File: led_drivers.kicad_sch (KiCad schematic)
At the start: 7 parts, among them Q1 MMBT3904

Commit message: routing done
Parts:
- renumbered Q1 to Q6, R4 to R43, R5 to R44, R6 to R45, R7 to R46, R8 to R47, R18 to R48
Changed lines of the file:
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@@
   (symbol (lib_id "Device:R") (at 109.22 59.055 0) (unit 1)
     (in_bom yes) (on_board yes) (fields_autoplaced)
-    (property "Reference" "R18" (id 0) (at 110.998 58.2203 0)
+    (property "Reference" "R48" (id 0) (at 110.998 58.2203 0)
       (effects (font (size 1.27 1.27)) (justify left))
     )
@@
   (symbol (lib_id "Device:R") (at 71.12 59.055 0) (unit 1)
     (in_bom yes) (on_board yes) (fields_autoplaced)
-    (property "Reference" "R5" (id 0) (at 72.898 58.2203 0)
+    (property "Reference" "R44" (id 0) (at 72.898 58.2203 0)
       (effects (font (size 1.27 1.27)) (justify left))
     )
@@
   (symbol (lib_id "Device:R") (at 59.69 67.945 90) (unit 1)
     (in_bom yes) (on_board yes) (fields_autoplaced)
-    (property "Reference" "R4" (id 0) (at 59.69 70.9914 90))
+    (property "Reference" "R43" (id 0) (at 59.69 70.9914 90))
     (property "Value" "5.1k" (id 1) (at 59.69 73.5283 90))
     (property "Footprint" "Resistor_SMD:R_0402_1005Metric" (id 2) (at 59.69 69.723 90)
@@
   (symbol (lib_id "Device:R") (at 80.645 59.055 0) (unit 1)
     (in_bom yes) (on_board yes) (fields_autoplaced)
-    (property "Reference" "R6" (id 0) (at 82.423 58.2203 0)
+    (property "Reference" "R45" (id 0) (at 82.423 58.2203 0)
       (effects (font (size 1.27 1.27)) (justify left))
     )
@@
   (symbol (lib_id "Transistor_BJT:MMBT3904") (at 68.58 67.945 0) (unit 1)
     (in_bom yes) (on_board yes) (fields_autoplaced)
-    (property "Reference" "Q1" (id 0) (at 73.4314 67.1103 0)
+    (property "Reference" "Q6" (id 0) (at 73.4314 67.1103 0)
       (effects (font (size 1.27 1.27)) (justify left))
     )
@@
   (symbol (lib_id "Device:R") (at 90.17 59.055 0) (unit 1)
     (in_bom yes) (on_board yes) (fields_autoplaced)
-    (property "Reference" "R7" (id 0) (at 91.948 58.2203 0)
+    (property "Reference" "R46" (id 0) (at 91.948 58.2203 0)
       (effects (font (size 1.27 1.27)) (justify left))
     )
@@
   (symbol (lib_id "power:VSS") (at 71.12 73.025 180) (unit 1)
     (in_bom yes) (on_board yes) (fields_autoplaced)
-    (property "Reference" "#PWR022" (id 0) (at 71.12 69.215 0)
+    (property "Reference" "#PWR057" (id 0) (at 71.12 69.215 0)
       (effects (font (size 1.27 1.27)) hide)
     )
@@
   (symbol (lib_id "Device:R") (at 99.695 59.055 0) (unit 1)
     (in_bom yes) (on_board yes) (fields_autoplaced)
-    (property "Reference" "R8" (id 0) (at 101.473 58.2203 0)
+    (property "Reference" "R47" (id 0) (at 101.473 58.2203 0)
       (effects (font (size 1.27 1.27)) (justify left))
     )

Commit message: ready to order
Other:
- note added: "Ib = 1mA Ic > 100mA @ Vge > 900mV Vce(sat) = 100mV @ Ic = 50mA"
- note removed: "Ib = 1mA Ic > 100mA @ Vge > 900mV Vce(sat) = 100mA @ Ic = 50mA"
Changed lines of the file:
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@@
     (effects (font (size 1.27 1.27)) (justify left bottom))
   )
-  (text "Ib = 1mA\nIc > 100mA @ Vge > 900mV\nVce(sat) = 100mA @ Ic = 50mA"
+  (text "Ib = 1mA\nIc > 100mA @ Vge > 900mV\nVce(sat) = 100mV @ Ic = 50mA"
     (at 76.2 77.47 0)
     (effects (font (size 1.27 1.27)) (justify left bottom))
@@
   (symbol (lib_id "power:VSS") (at 71.12 73.025 180) (unit 1)
     (in_bom yes) (on_board yes) (fields_autoplaced)
-    (property "Reference" "#PWR057" (id 0) (at 71.12 69.215 0)
+    (property "Reference" "#PWR059" (id 0) (at 71.12 69.215 0)
       (effects (font (size 1.27 1.27)) hide)
     )

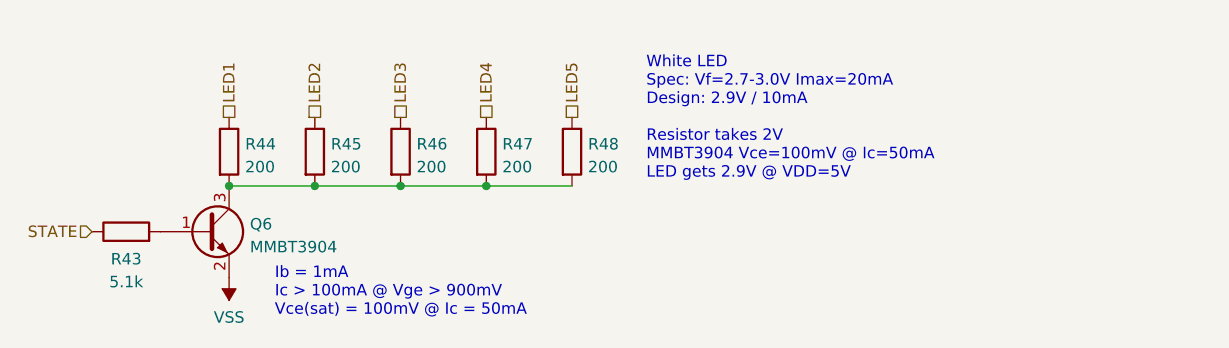
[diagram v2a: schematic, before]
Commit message: started fixing issues from V1
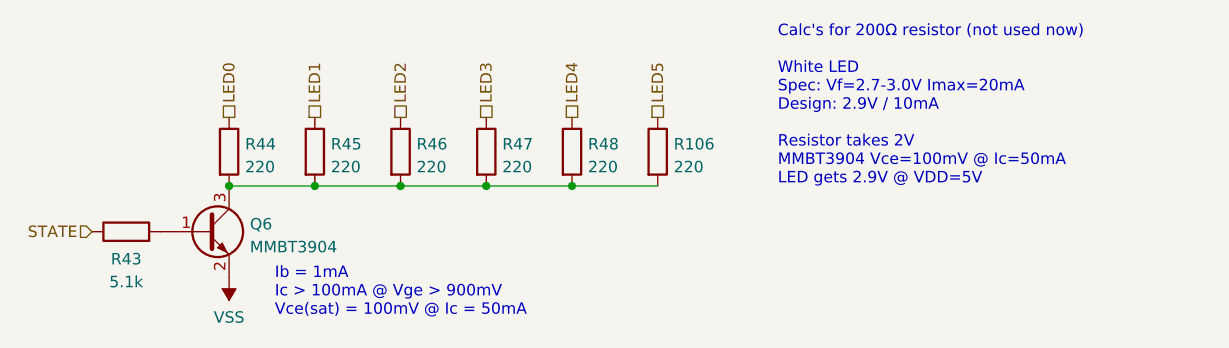
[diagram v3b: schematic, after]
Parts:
- added R106: 220, Resistor_SMD:R_0402_1005Metric, symbol Device:R
- R44, R45, R46, R47, R48: value 200 -> 220; JLC C25087 -> C25091
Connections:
- net LED1: now also R45.1; no longer R44.1
- net LED2: now also R46.1; no longer R45.1
- net LED3: now also R47.1; no longer R46.1
- net LED4: now also R48.1; no longer R47.1
- net LED5: now also R106.1; no longer R48.1
- net at Q6.3 (C), R44.2, R45.2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: now also R106.2
- new net LED0: R44.1
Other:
- note added: "Calc's for 200Ω resistor (not used now) White LED Spec: Vf=2.7-3.0V Imax=20mA Design: 2.9V / 10mA Resistor takes 2V MMBT3904 Vce=100mV @ Ic=50mA LED gets 2.9V @ VDD=5V"
- note removed: "White LED Spec: Vf=2.7-3.0V Imax=20mA Design: 2.9V / 10mA Resistor takes 2V MMBT3904 Vce=100mV @ Ic=50mA LED gets 2.9V @ VDD=5V"
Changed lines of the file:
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@@
   (junction (at 90.17 62.865) (diameter 0) (color 0 0 0 0)
   )
+  (junction (at 109.22 62.865) (diameter 0) (color 0 0 0 0)
+  )
   (wire (pts (xy 71.12 62.865) (xy 80.645 62.865))
     (stroke (width 0) (type default) (color 0 0 0 0))
@@
     (stroke (width 0) (type default) (color 0 0 0 0))
   )
+  (wire (pts (xy 109.22 62.865) (xy 118.745 62.865))
+    (stroke (width 0) (type default) (color 0 0 0 0))
+  )
   (wire (pts (xy 90.17 62.865) (xy 99.695 62.865))
     (stroke (width 0) (type default) (color 0 0 0 0))
@@
     (stroke (width 0) (type default) (color 0 0 0 0))
   )
-  (text "White LED\nSpec: Vf=2.7-3.0V Imax=20mA\nDesign: 2.9V / 10mA\n\nResistor takes 2V\nMMBT3904 Vce=100mV @ Ic=50mA\nLED gets 2.9V @ VDD=5V"
-    (at 117.475 62.23 0)
+  (text "Calc's for 200Ω resistor (not used now)\n\nWhite LED\nSpec: Vf=2.7-3.0V Imax=20mA\nDesign: 2.9V / 10mA\n\nResistor takes 2V\nMMBT3904 Vce=100mV @ Ic=50mA\nLED gets 2.9V @ VDD=5V"
+    (at 132.08 62.865 0)
     (effects (font (size 1.27 1.27)) (justify left bottom))
   )
@@
     (effects (font (size 1.27 1.27)) (justify left bottom))
   )
-  (hierarchical_label "LED2" (shape passive) (at 80.645 55.245 90)
-    (effects (font (size 1.27 1.27)) (justify left))
-  )
-  (hierarchical_label "LED1" (shape passive) (at 71.12 55.245 90)
-    (effects (font (size 1.27 1.27)) (justify left))
-  )
-  (hierarchical_label "LED5" (shape passive) (at 109.22 55.245 90)
-    (effects (font (size 1.27 1.27)) (justify left))
-  )
-  (hierarchical_label "LED3" (shape passive) (at 90.17 55.245 90)
+  (hierarchical_label "LED2" (shape passive) (at 90.17 55.245 90)
+    (effects (font (size 1.27 1.27)) (justify left))
+  )
+  (hierarchical_label "LED1" (shape passive) (at 80.645 55.245 90)
+    (effects (font (size 1.27 1.27)) (justify left))
+  )
+  (hierarchical_label "LED5" (shape passive) (at 118.745 55.245 90)
+    (effects (font (size 1.27 1.27)) (justify left))
+  )
+  (hierarchical_label "LED3" (shape passive) (at 99.695 55.245 90)
+    (effects (font (size 1.27 1.27)) (justify left))
+  )
+  (hierarchical_label "LED0" (shape passive) (at 71.12 55.245 90)
     (effects (font (size 1.27 1.27)) (justify left))
   )
@@
     (effects (font (size 1.27 1.27)) (justify right))
   )
-  (hierarchical_label "LED4" (shape passive) (at 99.695 55.245 90)
+  (hierarchical_label "LED4" (shape passive) (at 109.22 55.245 90)
     (effects (font (size 1.27 1.27)) (justify left))
   )
@@
       (effects (font (size 1.27 1.27)) (justify left))
     )
-    (property "Value" "200" (id 1) (at 110.998 60.7572 0)
+    (property "Value" "220" (id 1) (at 110.998 60.7572 0)
       (effects (font (size 1.27 1.27)) (justify left))
     )
@@
       (effects (font (size 1.27 1.27)) hide)
     )
-    (property "JLC" "C25087" (id 4) (at 109.22 59.055 0)
+    (property "JLC" "C25091" (id 4) (at 109.22 59.055 0)
       (effects (font (size 1.27 1.27)) hide)
     )
@@
       (effects (font (size 1.27 1.27)) (justify left))
     )
-    (property "Value" "200" (id 1) (at 72.898 60.7572 0)
+    (property "Value" "220" (id 1) (at 72.898 60.7572 0)
       (effects (font (size 1.27 1.27)) (justify left))
     )
@@
       (effects (font (size 1.27 1.27)) hide)
     )
-    (property "JLC" "C25087" (id 4) (at 71.12 59.055 0)
+    (property "JLC" "C25091" (id 4) (at 71.12 59.055 0)
       (effects (font (size 1.27 1.27)) hide)
     )
@@
     (pin "2")
   )
+  (symbol (lib_id "Device:R") (at 118.745 59.055 0) (unit 1)
+    (in_bom yes) (on_board yes) (fields_autoplaced)
+    (property "Reference" "R106" (id 0) (at 120.523 58.2203 0)
+      (effects (font (size 1.27 1.27)) (justify left))
+    )
+    (property "Value" "220" (id 1) (at 120.523 60.7572 0)
+      (effects (font (size 1.27 1.27)) (justify left))
+    )
+    (property "Footprint" "Resistor_SMD:R_0402_1005Metric" (id 2) (at 116.967 59.055 90)
+      (effects (font (size 1.27 1.27)) hide)
+    )
+    (property "Datasheet" "https://datasheet.lcsc.com/lcsc/2205311900_UNI-ROYAL-Uniroyal-Elec-0402WGF2000TCE_C25087.pdf" (id 3) (at 118.745 59.055 0)
+      (effects (font (size 1.27 1.27)) hide)
+    )
+    (property "JLC" "C25091" (id 4) (at 118.745 59.055 0)
+      (effects (font (size 1.27 1.27)) hide)
+    )
+    (pin "1")
+    (pin "2")
+  )
   (symbol (lib_id "Device:R") (at 80.645 59.055 0) (unit 1)
     (in_bom yes) (on_board yes) (fields_autoplaced)
@@
       (effects (font (size 1.27 1.27)) (justify left))
     )
-    (property "Value" "200" (id 1) (at 82.423 60.7572 0)
+    (property "Value" "220" (id 1) (at 82.423 60.7572 0)
       (effects (font (size 1.27 1.27)) (justify left))
     )
@@
       (effects (font (size 1.27 1.27)) hide)
     )
-    (property "JLC" "C25087" (id 4) (at 80.645 59.055 0)
+    (property "JLC" "C25091" (id 4) (at 80.645 59.055 0)
       (effects (font (size 1.27 1.27)) hide)
     )
@@
       (effects (font (size 1.27 1.27)) (justify left))
     )
-    (property "Value" "200" (id 1) (at 91.948 60.7572 0)
+    (property "Value" "220" (id 1) (at 91.948 60.7572 0)
       (effects (font (size 1.27 1.27)) (justify left))
     )
@@
       (effects (font (size 1.27 1.27)) hide)
     )
-    (property "JLC" "C25087" (id 4) (at 90.17 59.055 0)
+    (property "JLC" "C25091" (id 4) (at 90.17 59.055 0)
       (effects (font (size 1.27 1.27)) hide)
     )
@@
       (effects (font (size 1.27 1.27)) (justify left))
     )
-    (property "Value" "200" (id 1) (at 101.473 60.7572 0)
+    (property "Value" "220" (id 1) (at 101.473 60.7572 0)
       (effects (font (size 1.27 1.27)) (justify left))
     )
@@
       (effects (font (size 1.27 1.27)) hide)
     )
-    (property "JLC" "C25087" (id 4) (at 99.695 59.055 0)
-      (effects (font (size 1.27 1.27)) hide)
-    )
+    (property "JLC" "C25091" (id 4) (at 99.695 59.055 0)
+      (effects (font (size 1.27 1.27)) hide)
+    )
